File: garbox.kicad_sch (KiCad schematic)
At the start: 22 parts, among them J2 Speaker Terminals, J4 MSD-4-A, U1 ESP32-S3-WROOM-1-N4R8

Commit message: meant to put these in the last commit
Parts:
- removed C14: 10uF, CL31A106KBHNNNE:CAP_CL31_SAM, symbol CL31A106KBHNNNE:CL31A106KBHNNNE
- removed C18: 1uF, CL31B105KBHNNNE:CAPC3216X180N, symbol CL31B105KBHNNNE:CL31B105KBHNNNE
- removed C21: 100nF, CL05B224KO5NNNC:CAPC1005X55N, symbol CL05B104KO5NNNC:CL05B104KO5NNNC
- removed J2: Speaker Terminals, TerminalBlock_MetzConnect:TerminalBlock_MetzConnect_Type011_RT05502HBLC_1x02_P5.00mm_Horizontal, symbol Connector:Screw_Terminal_01x02
- removed J4: MSD-4-A, MSD_4_A:CUI_MSD-4-A, symbol MSD_4_A:MSD-4-A
- removed R25, R26, R27, R28, R29: 10k, Resistor_SMD:R_0201_0603Metric, symbol Device:R
- added J2: USB_Header, TS_110_G_A:SAMTEC_TS-110-G-A, symbol TS_110_G_A:TS-110-G-A
- added J5: SD_Header, TS_110_G_A:SAMTEC_TS-110-G-A, symbol TS_110_G_A:TS-110-G-A
- added J6: PowerBreakoutHeader, TS_110_G_A:SAMTEC_TS-110-G-A, symbol TS_110_G_A:TS-110-G-A
- added J7: BMS_Header, TS_110_G_A:SAMTEC_TS-110-G-A, symbol TS_110_G_A:TS-110-G-A
- added J8: Audio_Header, TS_110_G_A:SAMTEC_TS-110-G-A, symbol TS_110_G_A:TS-110-G-A
- added J9: GPIO_Header, TS_110_G_A:SAMTEC_TS-110-G-A, symbol TS_110_G_A:TS-110-G-A
- added R30, R31: 22, Resistor_SMD:R_0201_0603Metric, symbol Device:R
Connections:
- net USB_Data&Power/FLASH_TXD is gone; now on net FLASH_TXD: R16.1
- net +3.3V: now also J5.10, J6.01, J6.02
- net +5V: now also J6.09, J6.10
- net GND: now also J5.01, J5.02, J6.05, J6.06, J7.03, J7.04, J8.01, J8.03, J8.05
- net SD_CD: now also J5.09
- net SD_CLK: now also J5.06
- net SD_CMD: now also J5.05
- net SD_DAT0: now also J5.07
- net SD_DAT1: now also J5.08
- net SD_DAT2: now also J5.03
- net SD_DAT3: now also J5.04
- net at U1.13 (IO19): now also R30.1; no longer R23.1
- net GPLED_01: now reaches U1.10 (IO17)
- net GPLED_01: now also R23.1
- net GPLED_02: now reaches U1.11 (IO18)
- net GPLED_02: now also R8.1
- net GPIO_08: now reaches U1.12 (IO8)
- net GPIO_08: now also J9.01
- net at U1.14 (IO20): now also R31.1; no longer R8.1
- net GPIO_03: now reaches U1.15 (IO3)
- net GPIO_03: now also J9.02
- net GPIO_46: now reaches U1.16 (IO46)
- net GPIO_46: now also J9.03
- net GPIO_09: now reaches U1.17 (IO9)
- net GPIO_09: now also J9.04
- net GPIO_48: now reaches U1.25 (IO48)
- net GPIO_48: now also J9.05
- net GPIO_39: now reaches U1.32 (IO39)
- net GPIO_39: now also J9.06
- net GPIO_41: now reaches U1.34 (IO41)
- net GPIO_41: now also J9.07
- net GPIO_42: now reaches U1.35 (IO42)
- net GPIO_42: now also J9.08
- net GPIO_02: now reaches U1.38 (IO2)
- net GPIO_02: now also J9.09
- net GPIO_01: now reaches U1.39 (IO1)
- net GPIO_01: now also J9.10
- net Audio/AMP_ENABLE renamed AMP_ENABLE
- net AMP_ENABLE: now also J8.06
- net Audio/i2s_LRCK renamed i2s_LRCK
- net i2s_LRCK: now also J8.08
- net Audio/i2s_MCLK renamed i2s_MCLK
- net i2s_MCLK: now also J8.07
- net Audio/i2s_SCLK renamed i2s_SCLK
- net i2s_SCLK: now also J8.09
- net Audio/i2s_SDIN renamed i2s_SDIN
- net i2s_SDIN: now also J8.10
- net BatteryManagement/BMS_Interrupt renamed BMS_Interrupt
- net BMS_Interrupt: now also J7.05
- net BatteryManagement/ChargeStatus renamed ChargeStatus
- net ChargeStatus: now also J7.08
- net BatteryManagement/PSEL renamed PSEL
- net PSEL: now also J7.06
- net BatteryManagement/PowerGood renamed PowerGood
- net PowerGood: now also J7.07
- net BatteryManagement/SCL renamed SCL
- net SCL: now also J7.10
- net BatteryManagement/SDA renamed SDA
- net SDA: now also J7.09
- net USB_Data&Power/CTS# renamed DTR#
- net DTR#: now also J2.06
- net USB_Data&Power/DTR# renamed FLASH_TXD
- net FLASH_TXD: now also J2.05, J2.07
- net USB_Data&Power/FLASH_RXD renamed FLASH_RXD
- net FLASH_RXD: now also J2.08
- net USB_Data&Power/RTS# renamed RTS#
- net RTS#: now also J2.09
- new net PowerRegulation/3V3: J6.03, J6.04
- new net PowerRegulation/5V: J6.07, J6.08
- new net Spk+: J8.04
- new net Spk-: J8.02
- new net USB_Data&Power/DCD#: J2.02
- new net USB_Data&Power/DSR#: J2.01
- new net USB_Data&Power/USB_Internal_D+: J2.04
- new net USB_Data&Power/USB_Internal_D-: J2.03
- new net USB_OTG_D+: J7.01, R31.2
- new net USB_OTG_D-: J7.02, R30.2
- new net USB_PowerSupply: J2.10
- no-connect marks 12 -> 1
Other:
- added sheet SD_Card (sdcard.kicad_sch)
- sheet USB_Data&Power ports: added DCD#, DSR#, RI#, USB_Internal_D+, USB_Internal_D-; removed none
- note added: "Note: DTR, RTS, CTS must be tied to specific GPIO Pins"
- note added: "USB OTG shouldn't be needed but I'll break it out just in case"
- note added: "internals only exposed for the header"
- note removed: "Note: DTR and CTS must be tied to specific GPIO Pins"
- note removed: "USB OTG?"
- note removed: "cap on EN?"
- note removed: "does it need a crystal?"
- note removed: "should we put a jtag header for redundancy?"
- moved on the sheet: C12, C25, C28, D3, D4, R1, R15, R16, R23, R7, R8, U1

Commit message: Finished preliminary routing of v1.1 of the board
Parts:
- added SW1: RotaryEncoder, Rotary_Encoder:RotaryEncoder_Bourns_Horizontal_PEC09-2xxxF-Nxxxx, symbol Device:RotaryEncoder
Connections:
- net +3.3V: now also J5.05; no longer J5.10
- net AMP_ENABLE: now also J8.07, U1.29 (IO36); no longer J8.06, U1.26 (IO45)
- net BMS_Interrupt: now also J7.08, U1.18 (IO10); no longer J7.05, U1.4 (IO4)
- net CTS#: now also J2.10, U1.33 (IO40)
- net ChargeStatus: now also J7.05, U1.21 (IO13); no longer J7.08, U1.7 (IO7)
- net DTR#: now also J2.05, U1.27 (IO0); no longer J2.06, U1.33 (IO40)
- net FLASH_RXD: now also J2.07; no longer J2.08
- net FLASH_TXD: now also J2.04; no longer J2.05, J2.07, U1.27 (IO0)
- net GND: now also J5.06, J7.01, J7.02, J8.09; no longer J5.02, J7.03, J7.04, J8.01, J8.03, J8.05
- net GPIO_03: now also J9.01; no longer J9.02
- net GPIO_08: now also J9.10, U1.4 (IO4); no longer J9.01, U1.12 (IO8)
- net GPIO_09: now also J9.03; no longer J9.04
- net GPIO_46: now also J9.02; no longer J9.03
- net GPLED_01: now also U1.12 (IO8); no longer U1.10 (IO17)
- net PSEL: now also J7.03, U1.23 (IO21); no longer J7.06, U1.9 (IO16)
- net PowerGood: now also J7.04, U1.22 (IO14); no longer J7.07, U1.8 (IO15)
- net RTS#: now also J2.06; no longer J2.09
- net SCL: now also J7.07, U1.19 (IO11); no longer J7.10, U1.5 (IO5)
- net SDA: now also J7.06, U1.20 (IO12); no longer J7.09, U1.6 (IO6)
- net SD_CD: now also J5.10, U1.30 (IO37); no longer J5.09, U1.18 (IO10)
- net SD_CLK: now also J5.07, U1.34 (IO41); no longer J5.06, U1.21 (IO13)
- net SD_CMD: now also J5.04, U1.35 (IO42); no longer J5.05, U1.22 (IO14)
- net SD_DAT0: now also J5.08, U1.32 (IO39); no longer J5.07, U1.20 (IO12)
- net SD_DAT1: now also J5.09, U1.31 (IO38); no longer J5.08, U1.19 (IO11)
- net SD_DAT2: now also J5.02, U1.39 (IO1); no longer J5.03, U1.24 (IO47)
- net SD_DAT3: now also J5.03, U1.38 (IO2); no longer J5.04, U1.23 (IO21)
- net Spk+: now also J8.10; no longer J8.04
- net Spk-: now also J8.08; no longer J8.02
- net USB_Data&Power/DCD#: now also J2.09; no longer J2.02
- net USB_Data&Power/DSR#: now also J2.08; no longer J2.01
- net USB_Data&Power/USB_Internal_D+: now also J2.02; no longer J2.04
- net USB_Data&Power/USB_Internal_D-: now also J2.01; no longer J2.03
- net USB_OTG_D+: now also J7.09; no longer J7.01
- net USB_OTG_D-: now also J7.10; no longer J7.02
- net USB_PowerSupply: now also J2.03; no longer J2.10
- net i2s_LRCK: now also J8.02, U1.25 (IO48); no longer J8.08, U1.29 (IO36)
- net i2s_MCLK: now also J8.01, U1.24 (IO47); no longer J8.07, U1.28 (IO35)
- net i2s_SCLK: now also J8.03, U1.26 (IO45); no longer J8.09, U1.30 (IO37)
- net i2s_SDIN: now also J8.04, U1.28 (IO35); no longer J8.10, U1.31 (IO38)
- removed net GPIO_01: J9.10, U1.39 (IO1)
- net GPIO_02 renamed GPIO_05
- net GPIO_05: now also U1.5 (IO5); no longer U1.38 (IO2)
- net GPIO_39 renamed GPIO_15
- net GPIO_15: now also U1.8 (IO15); no longer U1.32 (IO39)
- net GPIO_41 renamed GPIO_07
- net GPIO_07: now also U1.7 (IO7); no longer U1.34 (IO41)
- net GPIO_42 renamed GPIO_06
- net GPIO_06: now also U1.6 (IO6); no longer U1.35 (IO42)
- net GPIO_48 renamed GPIO_16
- net GPIO_16: now also U1.9 (IO16); no longer U1.25 (IO48)
- new net GPIO_17: J9.04, U1.10 (IO17)
- new net PostDac: J8.05
- new net PreAmp: J8.06
- no-connect marks 1 -> 0
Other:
- sheet Audio ports: added PostDAC, PreAmp; removed none
- note added: "Dummy component but with real datasheet of part we're using. This is for quick reference, but note that this component will not be mounted on the board"
- moved on the sheet: J5

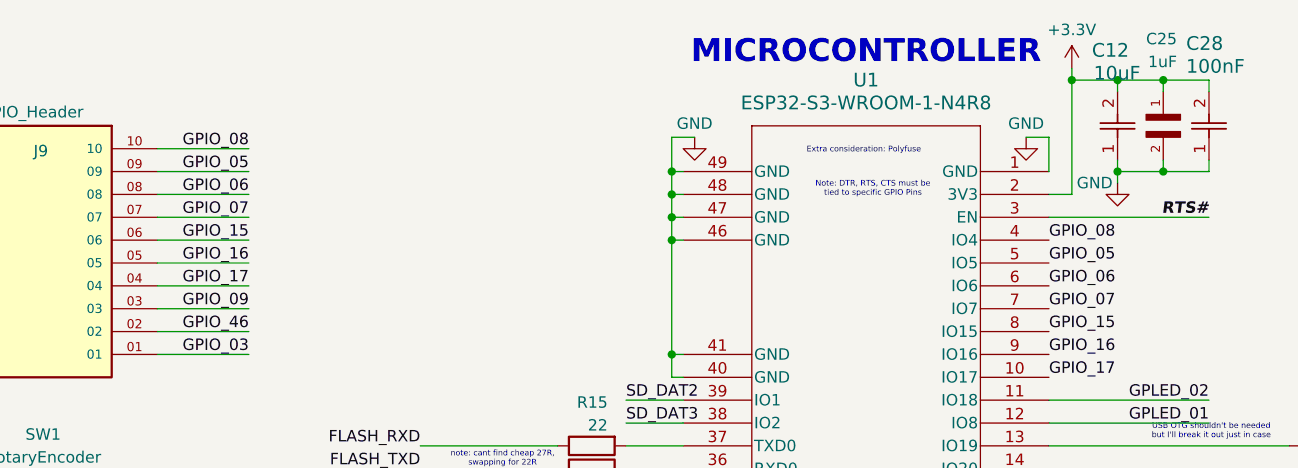
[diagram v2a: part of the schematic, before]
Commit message: fixed incorrect gpio and added silkscreen funny
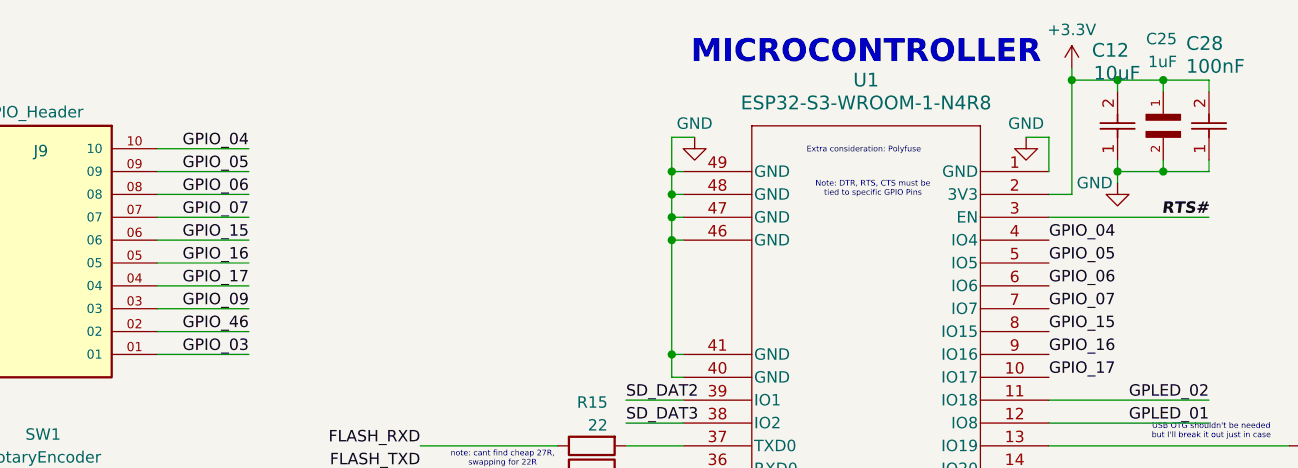
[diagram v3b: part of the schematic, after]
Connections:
- net GPIO_08 renamed GPIO_04
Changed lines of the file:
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@@
 		)
 	)
-	(label "GPIO_08"
+	(label "GPIO_04"
 		(at 151.13 40.64 0)
 		(effects
@@
 		)
 	)
-	(label "GPIO_08"
+	(label "GPIO_04"
 		(at 62.23 30.48 180)
 		(effects

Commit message: designated MPN parts from JLC library
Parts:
- C12: MPN (none) -> C13585
- C25: MPN (none) -> C1848
- C28: MPN (none) -> C1525
- D3, D4: MPN (none) -> C2286
- J2: MPN (none) -> C3333064
- J5, J6, J7, J8, J9: MPN (none) -> C57369
- R1, R7: MPN (none) -> C25804
- R15, R16, R30, R31: MPN (none) -> C23345
- R23, R8: MPN (none) -> C22966
- SW1: MPN (none) -> C143788
- U1: MPN (none) -> C2913200
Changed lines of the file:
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@@
+			)
+		)
+		(property "MPN" "C57369"
+			(at 26.67 173.99 0)
+			(effects
+				(font
+					(size 1.27 1.27)
+				)
+				(hide yes)
 			)
 		)
@@
 				)
 				(justify bottom)
+				(hide yes)
+			)
+		)
+		(property "MPN" "C3333064"
+			(at 26.67 133.35 0)
+			(effects
+				(font
+					(size 1.27 1.27)
+				)
 				(hide yes)
 			)
@@
 			)
 		)
+		(property "MPN" "C23345"
+			(at 181.61 63.5 90)
+			(effects
+				(font
+					(size 1.27 1.27)
+				)
+				(hide yes)
+			)
+		)
 		(pin "2"
 		)
@@
 				)
 				(justify bottom)
+				(hide yes)
+			)
+		)
+		(property "MPN" "C57369"
+			(at 203.2 96.52 0)
+			(effects
+				(font
+					(size 1.27 1.27)
+				)
 				(hide yes)
 			)
@@
 			)
 		)
+		(property "MPN" "C1848"
+			(at 163.83 26.67 90)
+			(effects
+				(font
+					(size 1.27 1.27)
+				)
+				(hide yes)
+			)
+		)
 		(pin "2"
 		)
@@
 			)
 		)
+		(property "MPN" "C57369"
+			(at 147.32 125.73 0)
+			(effects
+				(font
+					(size 1.27 1.27)
+				)
+				(hide yes)
+			)
+		)
 		(pin "01"
 		)
@@
 			)
 		)
+		(property "MPN" "C23345"
+			(at 100.33 66.04 90)
+			(effects
+				(font
+					(size 1.27 1.27)
+				)
+				(hide yes)
+			)
+		)
 		(pin "2"
 		)
@@
 			)
 		)
+		(property "MPN" "C22966"
+			(at 204.47 50.8 90)
+			(effects
+				(font
+					(size 1.27 1.27)
+				)
+				(hide yes)
+			)
+		)
 		(pin "2"
 		)
@@
 		(property "Description" "0603WAF220JT5E"
 			(at 181.61 66.04 0)
+			(effects
+				(font
+					(size 1.27 1.27)
+				)
+				(hide yes)
+			)
+		)
+		(property "MPN" "C23345"
+			(at 181.61 66.04 90)
 			(effects
 				(font
@@
 			)
 		)
+		(property "MPN" "C143788"
+			(at 39.37 72.39 0)
+			(effects
+				(font
+					(size 1.27 1.27)
+				)
+				(hide yes)
+			)
+		)
 		(pin "B"
 		)
@@
 		(property "Description" "0603WAF1002T5E"
 			(at 189.23 128.27 0)
+			(effects
+				(font
+					(size 1.27 1.27)
+				)
+				(hide yes)
+			)
+		)
+		(property "MPN" "C25804"
+			(at 189.23 128.27 90)
 			(effects
 				(font
@@
 			)
 		)
+		(property "MPN" "C57369"
+			(at 119.38 170.18 0)
+			(effects
+				(font
+					(size 1.27 1.27)
+				)
+				(hide yes)
+			)
+		)
 		(pin "01"
 		)
@@
 			)
 		)
+		(property "MPN" "C2286"
+			(at 212.09 50.8 0)
+			(effects
+				(font
+					(size 1.27 1.27)
+				)
+				(hide yes)
+			)
+		)
 		(pin "1"
 		)
@@
 			)
 		)
+		(property "MPN" "C57369"
+			(at 39.37 40.64 0)
+			(effects
+				(font
+					(size 1.27 1.27)
+				)
+				(hide yes)
+			)
+		)
 		(pin "01"
 		)
@@
 			)
 		)
+		(property "MPN" "C13585"
+			(at 158.75 31.75 90)
+			(effects
+				(font
+					(size 1.27 1.27)
+				)
+				(hide yes)
+			)
+		)
 		(pin "2"
 		)
@@
 		(property "Description" "CL05B104KO5NNNC"
 			(at 168.91 31.75 0)
+			(effects
+				(font
+					(size 1.27 1.27)
+				)
+				(hide yes)
+			)
+		)
+		(property "MPN" "C1525"
+			(at 168.91 31.75 90)
 			(effects
 				(font
@@
 			)
 		)
+		(property "MPN" "C23345"
+			(at 100.33 63.5 90)
+			(effects
+				(font
+					(size 1.27 1.27)
+				)
+				(hide yes)
+			)
+		)
 		(pin "2"
 		)
@@
 			)
 		)
+		(property "MPN" "C2913200"
+			(at 151.13 33.02 0)
+			(effects
+				(font
+					(size 1.27 1.27)
+				)
+				(hide yes)
+			)
+		)
 		(pin "39"
 		)
@@
 			)
 		)
+		(property "MPN" "C25804"
+			(at 196.85 128.27 90)
+			(effects
+				(font
+					(size 1.27 1.27)
+				)
+				(hide yes)
+			)
+		)
 		(pin "2"
 		)
@@
 			)
 		)
+		(property "MPN" "C22966"
+			(at 204.47 58.42 90)
+			(effects
+				(font
+					(size 1.27 1.27)
+				)
+				(hide yes)
+			)
+		)
 		(pin "2"
 		)
@@
 			(at 212.09 58.42 0)
 			(effects
+				(font
+					(size 1.27 1.27)
+				)
+				(hide yes)
+			)
+		)
+		(property "MPN" "C2286"
+			(at 212.09 58.42 0)
+			(effects
